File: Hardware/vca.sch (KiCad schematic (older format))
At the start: 20 parts

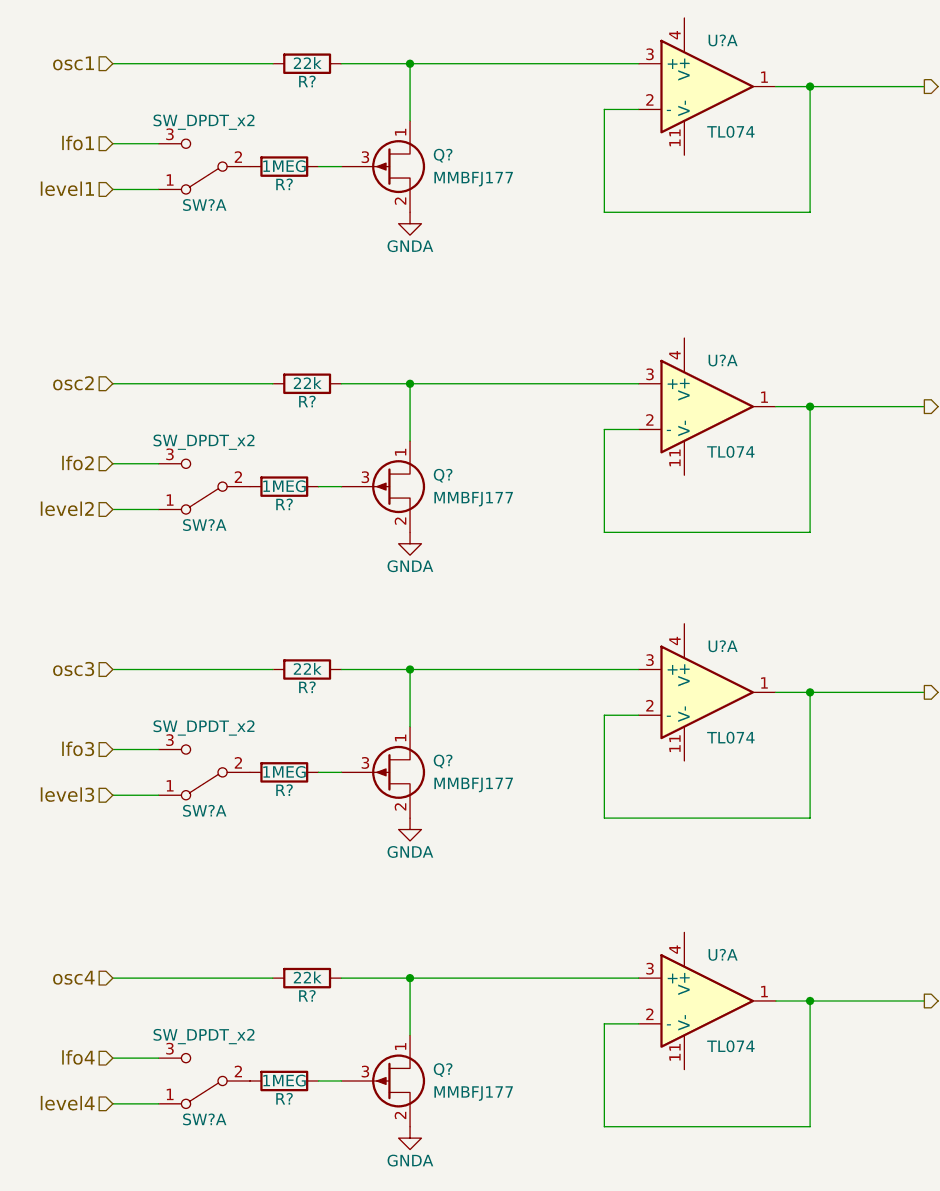
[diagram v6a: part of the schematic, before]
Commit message: add power jack, 3.3V regulator, VREF divider
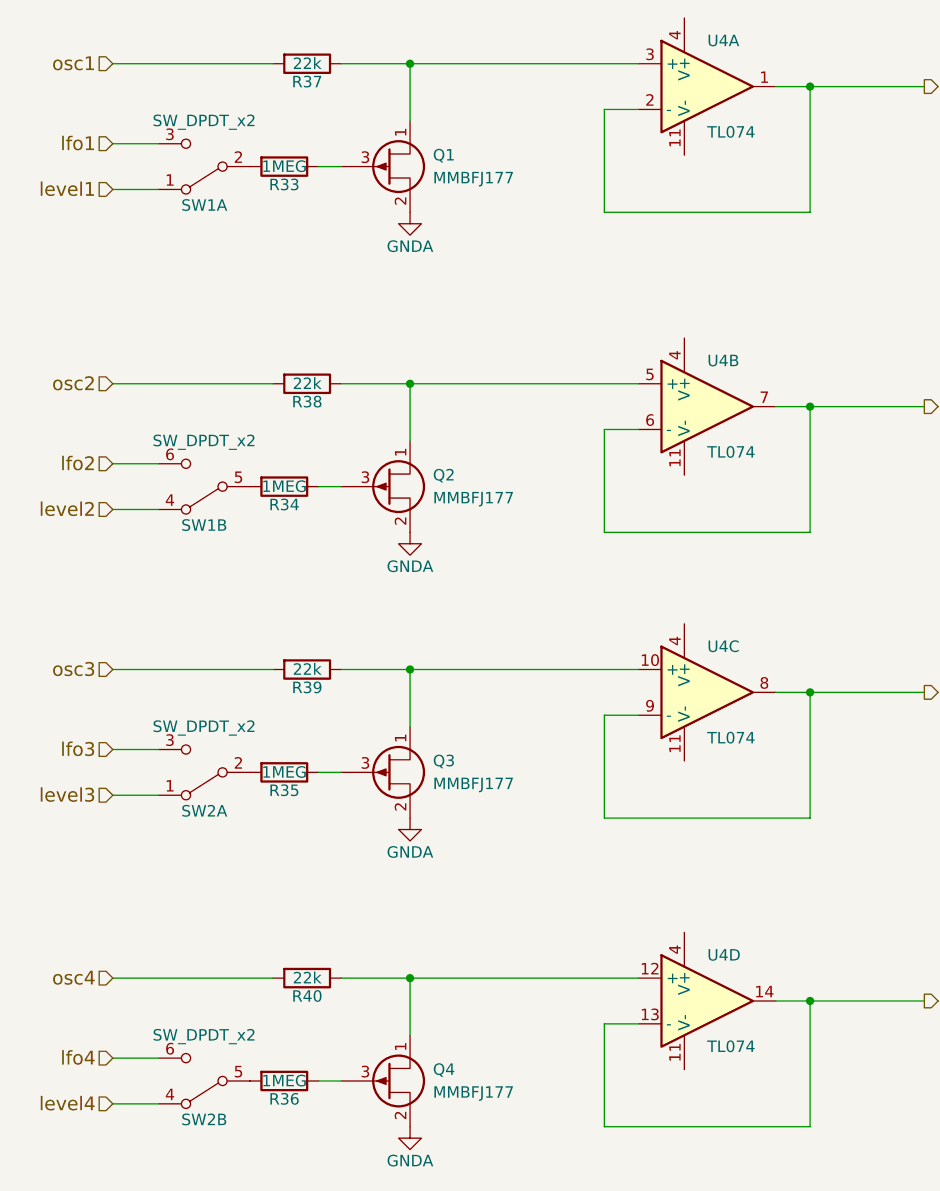
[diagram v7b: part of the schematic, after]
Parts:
- gave numbers to parts that had none: 15
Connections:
- net env_out_2: now also U4.6 (-), U4.7; no longer U4.1, U4.2 (-)
- net env_out_3: now also U4.8, U4.9 (-); no longer U4.1, U4.2 (-)
- net env_out_4: now also U4.13 (-), U4.14; no longer U4.1, U4.2 (-)
- net level2: now also SW1.4 (A); no longer SW1.1 (A)
- net level4: now also SW2.4 (A); no longer SW2.1 (A)
- net lfo2: now also SW1.6 (C); no longer SW1.3 (C)
- net lfo4: now also SW2.6 (C); no longer SW2.3 (C)
- net at Q2.1 (D), R38.1: now also U4.5 (+); no longer U4.3 (+)
- net at R34.2: now also SW1.5 (B); no longer SW1.2 (B)
- net at Q3.1 (D), R39.1: now also U4.10 (+); no longer U4.3 (+)
- net at Q4.1 (D), R40.1: now also U4.12 (+); no longer U4.3 (+)
- net at R36.2: now also SW2.5 (B); no longer SW2.2 (B)
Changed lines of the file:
@@
 osc1
 $Comp
-L Q_PJFET_DSG Q?
+L Q_PJFET_DSG Q1
 U 1 1 5C359797
 P 4450 1400
-F 0 "Q?" H 4650 1450 50  0000 L CNN
+F 0 "Q1" H 4650 1450 50  0000 L CNN
 F 1 "MMBFJ177" H 4650 1350 50  0000 L CNN
 F 2 "" H 4650 1500 50  0001 C CNN
@@
 $EndComp
 $Comp
-L R R?
+L R R37
 U 1 1 5C359814
 P 4100 950
-F 0 "R?" V 4180 950 50  0000 C CNN
+F 0 "R37" V 4180 950 50  0000 C CNN
 F 1 "22k" V 4100 950 50  0000 C CNN
 F 2 "" V 4030 950 50  0001 C CNN
@@
 $EndComp
 $Comp
-L TL074 U?
+L TL074 U4
 U 1 1 5C359D57
 P 5850 1050
-F 0 "U?" H 5850 1250 50  0000 L CNN
+F 0 "U4" H 5850 1250 50  0000 L CNN
 F 1 "TL074" H 5850 850 50  0000 L CNN
 F 2 "" H 5800 1150 50  0001 C CNN
@@
 	5400 1150 5550 1150
 $Comp
-L GNDA #PWR?
+L GNDA #PWR37
 U 1 1 5C359DD5
 P 4550 1600
-F 0 "#PWR?" H 4550 1350 50  0001 C CNN
+F 0 "#PWR37" H 4550 1350 50  0001 C CNN
 F 1 "GNDA" H 4550 1450 50  0000 C CNN
 F 2 "" H 4550 1600 50  0001 C CNN
@@
 	4550 1200 4550 950
 $Comp
-L R R?
+L R R33
 U 1 1 5C359EAD
 P 4000 1400
-F 0 "R?" V 4080 1400 50  0000 C CNN
+F 0 "R33" V 4080 1400 50  0000 C CNN
 F 1 "1MEG" V 4000 1400 50  0000 C CNN
 F 2 "" V 3930 1400 50  0001 C CNN
@@
 level1
 $Comp
-L SW_DPDT_x2 SW?
+L SW_DPDT_x2 SW1
 U 1 1 5C35A0BC
 P 3650 1400
-F 0 "SW?" H 3650 1570 50  0000 C CNN
+F 0 "SW1" H 3650 1570 50  0000 C CNN
 F 1 "SW_DPDT_x2" H 3650 1200 50  0000 C CNN
 F 2 "" H 3650 1400 50  0001 C CNN
@@
 osc2
 $Comp
-L Q_PJFET_DSG Q?
+L Q_PJFET_DSG Q2
 U 1 1 5C36E8D9
 P 4450 2800
-F 0 "Q?" H 4650 2850 50  0000 L CNN
+F 0 "Q2" H 4650 2850 50  0000 L CNN
 F 1 "MMBFJ177" H 4650 2750 50  0000 L CNN
 F 2 "" H 4650 2900 50  0001 C CNN
@@
 $EndComp
 $Comp
-L R R?
+L R R38
 U 1 1 5C36E8DF
 P 4100 2350
-F 0 "R?" V 4180 2350 50  0000 C CNN
+F 0 "R38" V 4180 2350 50  0000 C CNN
 F 1 "22k" V 4100 2350 50  0000 C CNN
 F 2 "" V 4030 2350 50  0001 C CNN
@@
 $EndComp
 $Comp
-L TL074 U?
-U 1 1 5C36E8E5
+L TL074 U4
+U 2 1 5C36E8E5
 P 5850 2450
-F 0 "U?" H 5850 2650 50  0000 L CNN
+F 0 "U4" H 5850 2650 50  0000 L CNN
 F 1 "TL074" H 5850 2250 50  0000 L CNN
 F 2 "" H 5800 2550 50  0001 C CNN
 F 3 "" H 5900 2650 50  0001 C CNN
-	1    5850 2450
+	2    5850 2450
 	1    0    0    -1
 $EndComp
@@
 	5400 2550 5550 2550
 $Comp
-L GNDA #PWR?
+L GNDA #PWR38
 U 1 1 5C36E8F0
 P 4550 3000
-F 0 "#PWR?" H 4550 2750 50  0001 C CNN
+F 0 "#PWR38" H 4550 2750 50  0001 C CNN
 F 1 "GNDA" H 4550 2850 50  0000 C CNN
 F 2 "" H 4550 3000 50  0001 C CNN
@@
 	4550 2600 4550 2350
 $Comp
-L R R?
+L R R34
 U 1 1 5C36E8F9
 P 4000 2800
-F 0 "R?" V 4080 2800 50  0000 C CNN
+F 0 "R34" V 4080 2800 50  0000 C CNN
 F 1 "1MEG" V 4000 2800 50  0000 C CNN
 F 2 "" V 3930 2800 50  0001 C CNN
@@
 level2
 $Comp
-L SW_DPDT_x2 SW?
-U 1 1 5C36E903
+L SW_DPDT_x2 SW1
+U 2 1 5C36E903
 P 3650 2800
-F 0 "SW?" H 3650 2970 50  0000 C CNN
+F 0 "SW1" H 3650 2970 50  0000 C CNN
 F 1 "SW_DPDT_x2" H 3650 2600 50  0000 C CNN
 F 2 "" H 3650 2800 50  0001 C CNN
 F 3 "" H 3650 2800 50  0001 C CNN
-	1    3650 2800
+	2    3650 2800
 	-1   0    0    1
 $EndComp
@@
 osc3
 $Comp
-L Q_PJFET_DSG Q?
+L Q_PJFET_DSG Q3
 U 1 1 5C36E9D1
 P 4450 4050
-F 0 "Q?" H 4650 4100 50  0000 L CNN
+F 0 "Q3" H 4650 4100 50  0000 L CNN
 F 1 "MMBFJ177" H 4650 4000 50  0000 L CNN
 F 2 "" H 4650 4150 50  0001 C CNN
@@
 $EndComp
 $Comp
-L R R?
+L R R39
 U 1 1 5C36E9D7
 P 4100 3600
-F 0 "R?" V 4180 3600 50  0000 C CNN
+F 0 "R39" V 4180 3600 50  0000 C CNN
 F 1 "22k" V 4100 3600 50  0000 C CNN
 F 2 "" V 4030 3600 50  0001 C CNN
@@
 $EndComp
 $Comp
-L TL074 U?
-U 1 1 5C36E9DD
+L TL074 U4
+U 3 1 5C36E9DD
 P 5850 3700
-F 0 "U?" H 5850 3900 50  0000 L CNN
+F 0 "U4" H 5850 3900 50  0000 L CNN
 F 1 "TL074" H 5850 3500 50  0000 L CNN
 F 2 "" H 5800 3800 50  0001 C CNN
 F 3 "" H 5900 3900 50  0001 C CNN
-	1    5850 3700
+	3    5850 3700
 	1    0    0    -1
 $EndComp
@@
 	5400 3800 5550 3800
 $Comp
-L GNDA #PWR?
+L GNDA #PWR39
 U 1 1 5C36E9E8
 P 4550 4250
-F 0 "#PWR?" H 4550 4000 50  0001 C CNN
+F 0 "#PWR39" H 4550 4000 50  0001 C CNN
 F 1 "GNDA" H 4550 4100 50  0000 C CNN
 F 2 "" H 4550 4250 50  0001 C CNN
@@
 	4550 3850 4550 3600
 $Comp
-L R R?
+L R R35
 U 1 1 5C36E9F1
 P 4000 4050
-F 0 "R?" V 4080 4050 50  0000 C CNN
+F 0 "R35" V 4080 4050 50  0000 C CNN
 F 1 "1MEG" V 4000 4050 50  0000 C CNN
 F 2 "" V 3930 4050 50  0001 C CNN
@@
 level3
 $Comp
-L SW_DPDT_x2 SW?
+L SW_DPDT_x2 SW2
 U 1 1 5C36E9FB
 P 3650 4050
-F 0 "SW?" H 3650 4220 50  0000 C CNN
+F 0 "SW2" H 3650 4220 50  0000 C CNN
 F 1 "SW_DPDT_x2" H 3650 3850 50  0000 C CNN
 F 2 "" H 3650 4050 50  0001 C CNN
@@
 osc4
 $Comp
-L Q_PJFET_DSG Q?
+L Q_PJFET_DSG Q4
 U 1 1 5C36EAC9
 P 4450 5400
-F 0 "Q?" H 4650 5450 50  0000 L CNN
+F 0 "Q4" H 4650 5450 50  0000 L CNN
 F 1 "MMBFJ177" H 4650 5350 50  0000 L CNN
 F 2 "" H 4650 5500 50  0001 C CNN
@@
 $EndComp
 $Comp
-L R R?
+L R R40
 U 1 1 5C36EACF
 P 4100 4950
-F 0 "R?" V 4180 4950 50  0000 C CNN
+F 0 "R40" V 4180 4950 50  0000 C CNN
 F 1 "22k" V 4100 4950 50  0000 C CNN
 F 2 "" V 4030 4950 50  0001 C CNN
@@
 $EndComp
 $Comp
-L TL074 U?
-U 1 1 5C36EAD5
+L TL074 U4
+U 4 1 5C36EAD5
 P 5850 5050
-F 0 "U?" H 5850 5250 50  0000 L CNN
+F 0 "U4" H 5850 5250 50  0000 L CNN
 F 1 "TL074" H 5850 4850 50  0000 L CNN
 F 2 "" H 5800 5150 50  0001 C CNN
 F 3 "" H 5900 5250 50  0001 C CNN
-	1    5850 5050
+	4    5850 5050
 	1    0    0    -1
 $EndComp
@@
 	5400 5150 5550 5150
 $Comp
-L GNDA #PWR?
+L GNDA #PWR40
 U 1 1 5C36EAE0
 P 4550 5600
-F 0 "#PWR?" H 4550 5350 50  0001 C CNN
+F 0 "#PWR40" H 4550 5350 50  0001 C CNN
 F 1 "GNDA" H 4550 5450 50  0000 C CNN
 F 2 "" H 4550 5600 50  0001 C CNN
@@
 	4550 5200 4550 4950
 $Comp
-L R R?
+L R R36
 U 1 1 5C36EAE9
 P 4000 5400
-F 0 "R?" V 4080 5400 50  0000 C CNN
+F 0 "R36" V 4080 5400 50  0000 C CNN
 F 1 "1MEG" V 4000 5400 50  0000 C CNN
 F 2 "" V 3930 5400 50  0001 C CNN
@@
 level4
 $Comp
-L SW_DPDT_x2 SW?
-U 1 1 5C36EAF3
+L SW_DPDT_x2 SW2
+U 2 1 5C36EAF3
 P 3650 5400
-F 0 "SW?" H 3650 5570 50  0000 C CNN
+F 0 "SW2" H 3650 5570 50  0000 C CNN
 F 1 "SW_DPDT_x2" H 3650 5200 50  0000 C CNN
 F 2 "" H 3650 5400 50  0001 C CNN
 F 3 "" H 3650 5400 50  0001 C CNN
-	1    3650 5400
+	2    3650 5400
 	-1   0    0    1
 $EndComp

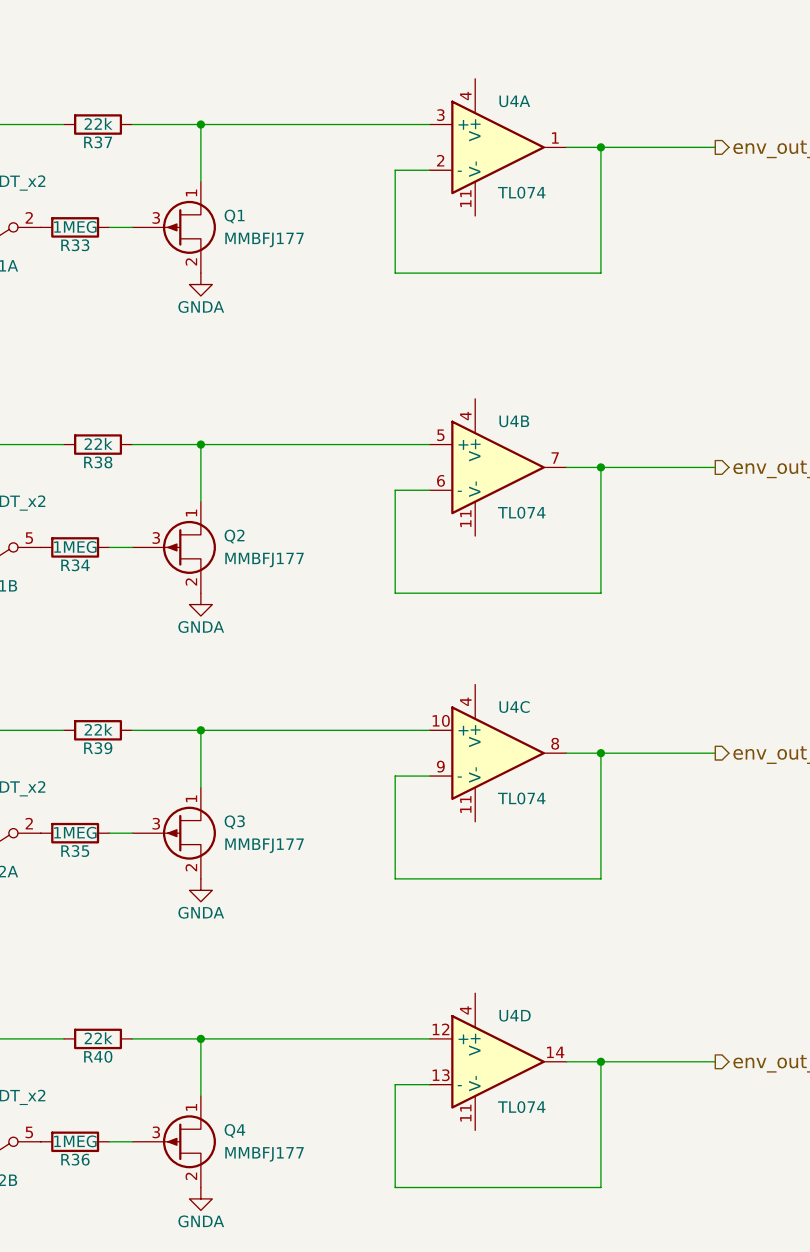
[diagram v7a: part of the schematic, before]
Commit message: add VREF to all single supply op amps
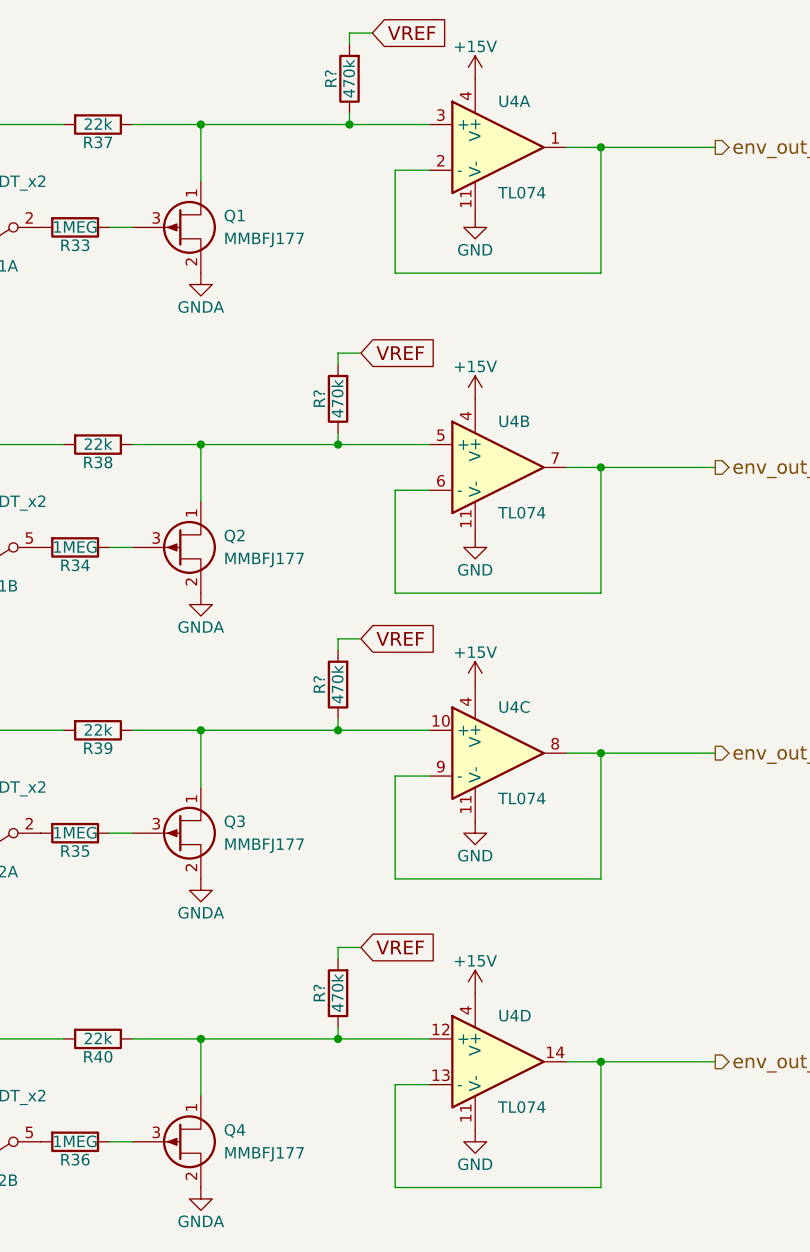
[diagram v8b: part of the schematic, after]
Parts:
- added R? (x4): 470k, symbol R
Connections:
- net at Q1.1 (D), R37.1, U4.3 (+): now also R?.1
- net GND: now reaches U4.11 (V-)
- net GND: now also U4.11 (V-), U4.11 (V-), U4.11 (V-)
- net +15V: now reaches U4.4 (V+)
- net +15V: now also U4.4 (V+), U4.4 (V+), U4.4 (V+)
- net at Q2.1 (D), R38.1, U4.5 (+): now also R?.1
- net at Q3.1 (D), R39.1, U4.10 (+): now also R?.1
- net at Q4.1 (D), R40.1, U4.12 (+): now also R?.1
- new net VREF: R?.2, R?.2, R?.2, R?.2
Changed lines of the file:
@@
 $Descr A4 11693 8268
 encoding utf-8
-Sheet 4 8
+Sheet 4 7
 Title ""
 Date ""
@@
 env_out_4
 Connection ~ 6300 5050
+$Comp
+L GND #PWR?
+U 1 1 5C39517B
+P 5750 1350
+F 0 "#PWR?" H 5750 1100 50  0001 C CNN
+F 1 "GND" H 5750 1200 50  0000 C CNN
+F 2 "" H 5750 1350 50  0001 C CNN
+F 3 "" H 5750 1350 50  0001 C CNN
+	1    5750 1350
+	1    0    0    -1
+$EndComp
+$Comp
+L GND #PWR?
+U 1 1 5C3951C9
+P 5750 2750
+F 0 "#PWR?" H 5750 2500 50  0001 C CNN
+F 1 "GND" H 5750 2600 50  0000 C CNN
+F 2 "" H 5750 2750 50  0001 C CNN
+F 3 "" H 5750 2750 50  0001 C CNN
+	1    5750 2750
+	1    0    0    -1
+$EndComp
+$Comp
+L GND #PWR?
+U 1 1 5C395210
+P 5750 4000
+F 0 "#PWR?" H 5750 3750 50  0001 C CNN
+F 1 "GND" H 5750 3850 50  0000 C CNN
+F 2 "" H 5750 4000 50  0001 C CNN
+F 3 "" H 5750 4000 50  0001 C CNN
+	1    5750 4000
+	1    0    0    -1
+$EndComp
+$Comp
+L GND #PWR?
+U 1 1 5C39530B
+P 5750 5350
+F 0 "#PWR?" H 5750 5100 50  0001 C CNN
+F 1 "GND" H 5750 5200 50  0000 C CNN
+F 2 "" H 5750 5350 50  0001 C CNN
+F 3 "" H 5750 5350 50  0001 C CNN
+	1    5750 5350
+	1    0    0    -1
+$EndComp
+$Comp
+L +15V #PWR?
+U 1 1 5C3953F4
+P 5750 750
+F 0 "#PWR?" H 5750 600 50  0001 C CNN
+F 1 "+15V" H 5750 890 50  0000 C CNN
+F 2 "" H 5750 750 50  0001 C CNN
+F 3 "" H 5750 750 50  0001 C CNN
+	1    5750 750
+	1    0    0    -1
+$EndComp
+$Comp
+L +15V #PWR?
+U 1 1 5C395442
+P 5750 2150
+F 0 "#PWR?" H 5750 2000 50  0001 C CNN
+F 1 "+15V" H 5750 2290 50  0000 C CNN
+F 2 "" H 5750 2150 50  0001 C CNN
+F 3 "" H 5750 2150 50  0001 C CNN
+	1    5750 2150
+	1    0    0    -1
+$EndComp
+$Comp
+L +15V #PWR?
+U 1 1 5C395489
+P 5750 3400
+F 0 "#PWR?" H 5750 3250 50  0001 C CNN
+F 1 "+15V" H 5750 3540 50  0000 C CNN
+F 2 "" H 5750 3400 50  0001 C CNN
+F 3 "" H 5750 3400 50  0001 C CNN
+	1    5750 3400
+	1    0    0    -1
+$EndComp
+$Comp
+L +15V #PWR?
+U 1 1 5C3954D0
+P 5750 4750
+F 0 "#PWR?" H 5750 4600 50  0001 C CNN
+F 1 "+15V" H 5750 4890 50  0000 C CNN
+F 2 "" H 5750 4750 50  0001 C CNN
+F 3 "" H 5750 4750 50  0001 C CNN
+	1    5750 4750
+	1    0    0    -1
+$EndComp
+$Comp
+L R R?
+U 1 1 5C395657
+P 5200 750
+F 0 "R?" V 5280 750 50  0000 C CNN
+F 1 "470k" V 5200 750 50  0000 C CNN
+F 2 "" V 5130 750 50  0001 C CNN
+F 3 "" H 5200 750 50  0001 C CNN
+	1    5200 750
+	-1   0    0    1
+$EndComp
+Wire Wire Line
+	5200 900  5200 950
+Connection ~ 5200 950
+Text GLabel 5300 550  2    60   Input ~ 0
+VREF
+Wire Wire Line
+	5300 550  5200 550
+Wire Wire Line
+	5200 550  5200 600
+$Comp
+L R R?
+U 1 1 5C3959EE
+P 5150 2150
+F 0 "R?" V 5230 2150 50  0000 C CNN
+F 1 "470k" V 5150 2150 50  0000 C CNN
+F 2 "" V 5080 2150 50  0001 C CNN
+F 3 "" H 5150 2150 50  0001 C CNN
+	1    5150 2150
+	-1   0    0    1
+$EndComp
+Text GLabel 5250 1950 2    60   Input ~ 0
+VREF
+Wire Wire Line
+	5250 1950 5150 1950
+Wire Wire Line
+	5150 1950 5150 2000
+$Comp
+L R R?
+U 1 1 5C395A9C
+P 5150 3400
+F 0 "R?" V 5230 3400 50  0000 C CNN
+F 1 "470k" V 5150 3400 50  0000 C CNN
+F 2 "" V 5080 3400 50  0001 C CNN
+F 3 "" H 5150 3400 50  0001 C CNN
+	1    5150 3400
+	-1   0    0    1
+$EndComp
+Text GLabel 5250 3200 2    60   Input ~ 0
+VREF
+Wire Wire Line
+	5250 3200 5150 3200
+Wire Wire Line
+	5150 3200 5150 3250
+$Comp
+L R R?
+U 1 1 5C395B2D
+P 5150 4750
+F 0 "R?" V 5230 4750 50  0000 C CNN
+F 1 "470k" V 5150 4750 50  0000 C CNN
+F 2 "" V 5080 4750 50  0001 C CNN
+F 3 "" H 5150 4750 50  0001 C CNN
+	1    5150 4750
+	-1   0    0    1
+$EndComp
+Text GLabel 5250 4550 2    60   Input ~ 0
+VREF
+Wire Wire Line
+	5250 4550 5150 4550
+Wire Wire Line
+	5150 4550 5150 4600
+Wire Wire Line
+	5150 4900 5150 4950
+Connection ~ 5150 4950
+Wire Wire Line
+	5150 3550 5150 3600
+Connection ~ 5150 3600
+Wire Wire Line
+	5150 2300 5150 2350
+Connection ~ 5150 2350
 $EndSCHEMATC
